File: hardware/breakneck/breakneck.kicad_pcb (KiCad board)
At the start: 2 copper layers, 53.3 x 64 mm, 117 parts, among them J1 CONN_WEST, J10 GS2, J12 CONN_JTAG_6P, J15 GS2, J16 CONN_JST, J2 CONN_DEDI, J3 CONN_OLED, J4 USB_C_Rcpt_Min, J5 CONN_SOUTH, J6 CONN_EAST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

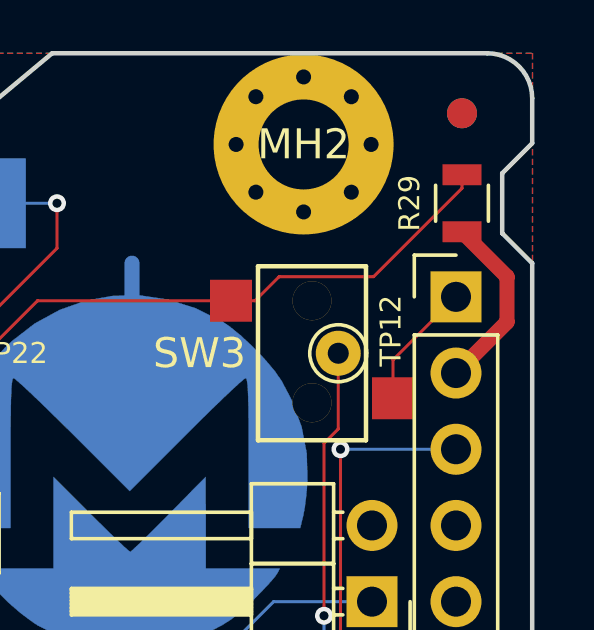
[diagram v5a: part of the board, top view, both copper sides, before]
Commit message: Corrected switching as VCI_IN0 is a wakeup or interrupt on active low.
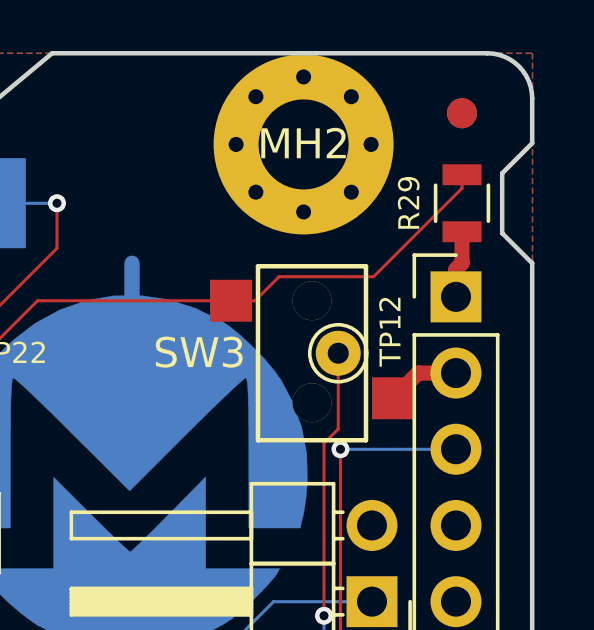
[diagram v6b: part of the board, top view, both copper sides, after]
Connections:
- R29 pad 1: +3V3 -> GND
- SW3 pad 2: GND -> +3V3
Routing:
- net +3V3: track 182.7 -> 179.1 mm
- net GND: track 226.8 -> 224.8 mm
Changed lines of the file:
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@@
     (fp_line (start 1.55 0.9) (end -1.55 0.9) (layer F.CrtYd) (width 0.05))
     (pad 1 smd rect (at -0.95 0 90) (size 0.7 1.3) (layers F.Cu F.Paste F.Mask)
-      (net 3 +3V3))
+      (net 1 GND))
     (pad 2 smd rect (at 0.95 0 90) (size 0.7 1.3) (layers F.Cu F.Paste F.Mask)
       (net 161 "Net-(R29-Pad2)"))
@@
       (net 161 "Net-(R29-Pad2)"))
     (pad 2 smd rect (at -1.5 2.7 90) (size 1.4 1.4) (layers F.Cu F.Paste F.Mask)
-      (net 1 GND))
+      (net 3 +3V3))
     (pad A thru_hole circle (at -1.65 0 90) (size 1.3 1.3) (drill 1.3) (layers *.Cu *.Mask))
     (pad B thru_hole circle (at 1.75 0 90) (size 1.3 1.3) (drill 1.3) (layers *.Cu *.Mask))
@@
   (segment (start 147 114.6) (end 147 113.5) (width 0.1016) (layer F.Cu) (net 1))
   (segment (start 144.5 114.6) (end 144.5 113.5) (width 0.1016) (layer F.Cu) (net 1))
-  (segment (start 148.7 75.5) (end 148.7 74.22) (width 0.1016) (layer F.Cu) (net 1))
-  (segment (start 148.7 74.22) (end 150.8 72.12) (width 0.1016) (layer F.Cu) (net 1))
   (segment (start 118.55 89.8726) (end 118.55 86.75) (width 0.508) (layer F.Cu) (net 1))
   (segment (start 123.6926 89.75) (end 125.045 91.1024) (width 0.1016) (layer B.Cu) (net 1))
@@
   (segment (start 146.75 123) (end 147 123.25) (width 0.1016) (layer B.Cu) (net 1))
   (segment (start 147.74 126.84) (end 147.74 123.99) (width 0.1016) (layer F.Cu) (net 1))
+  (segment (start 151 71) (end 151 69.95) (width 0.508) (layer F.Cu) (net 1))
+  (segment (start 150.8 72.12) (end 150.8 71.2) (width 0.508) (layer F.Cu) (net 1))
+  (segment (start 150.8 71.2) (end 151 71) (width 0.508) (layer F.Cu) (net 1))
   (via (at 132.8485 69) (size 0.6) (drill 0.3) (layers F.Cu B.Cu) (net 2))
   (segment (start 132.92 71.325) (end 132.92 69.0715) (width 0.1016) (layer B.Cu) (net 2) (status 10))
@@
   (segment (start 142.5 101.4) (end 141.352401 100.252401) (width 0.1016) (layer F.Cu) (net 3))
   (segment (start 141.352401 98.652401) (end 141.352401 101.897599) (width 0.1016) (layer F.Cu) (net 3))
-  (segment (start 150.8 74.66) (end 152.5 72.96) (width 0.508) (layer F.Cu) (net 3))
-  (segment (start 152.5 72.96) (end 152.5 71.45) (width 0.508) (layer F.Cu) (net 3))
-  (segment (start 152.5 71.45) (end 151 69.95) (width 0.508) (layer F.Cu) (net 3))
   (via (at 144.65 126.95) (size 0.6) (drill 0.3) (layers F.Cu B.Cu) (net 3))
   (segment (start 146 126.95) (end 144.65 126.95) (width 0.1016) (layer B.Cu) (net 3))
@@
   (segment (start 122.15 104.75) (end 122.5 105.1) (width 0.1016) (layer B.Cu) (net 3))
   (segment (start 118.114801 104.75) (end 122.15 104.75) (width 0.1016) (layer B.Cu) (net 3))
+  (segment (start 149.54 74.66) (end 148.7 75.5) (width 0.508) (layer F.Cu) (net 3))
+  (segment (start 150.8 74.66) (end 149.54 74.66) (width 0.508) (layer F.Cu) (net 3))
   (segment (start 139.5 112.4) (end 139.5 110.95) (width 0.1016) (layer F.Cu) (net 4) (status 30))
   (segment (start 119 80) (end 121.9976 77.0024) (width 0.1016) (layer B.Cu) (net 6) (status 10))

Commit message: Corrected incompatible SE (608A) timing in ROM assistance.
This follows advice taken from Microchip case 00347747, warning against
replacing the CEC1702 ROM addendum specification of ATECC508A with the
more capable ATECC608A SE.
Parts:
- U1: value ATECC608A -> ATECC508A
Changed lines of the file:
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@@
       (effects (font (size 1 1) (thickness 0.15)))
     )
-    (fp_text value ATECC608A (at 0 2.55 90) (layer F.Fab)
+    (fp_text value ATECC508A (at 0 2.55 90) (layer F.Fab)
       (effects (font (size 1 1) (thickness 0.15)))
     )

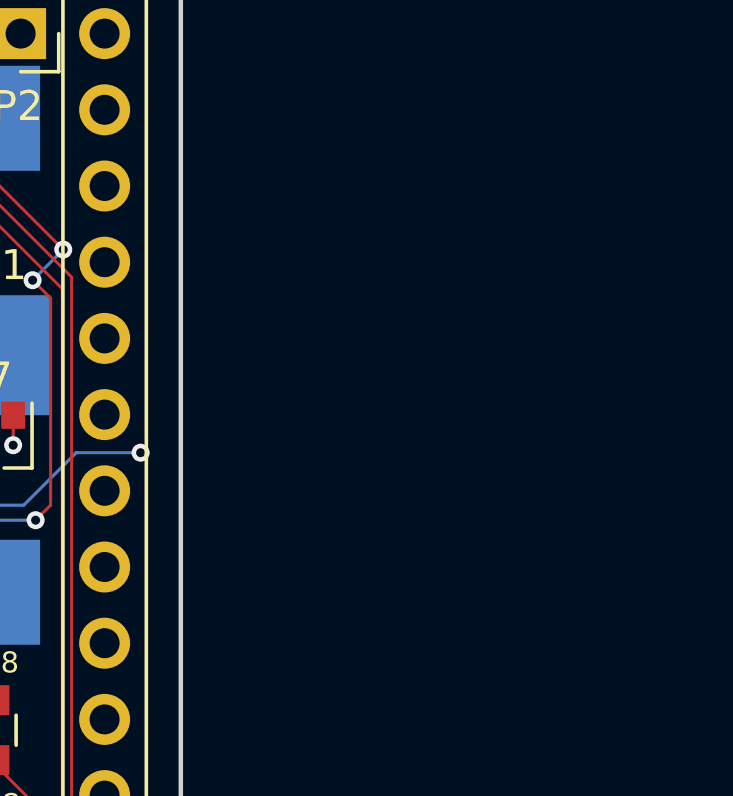
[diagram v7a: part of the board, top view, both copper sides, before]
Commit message: Prepared to integrate adjustable regulator and cleaned jumpers of paste.
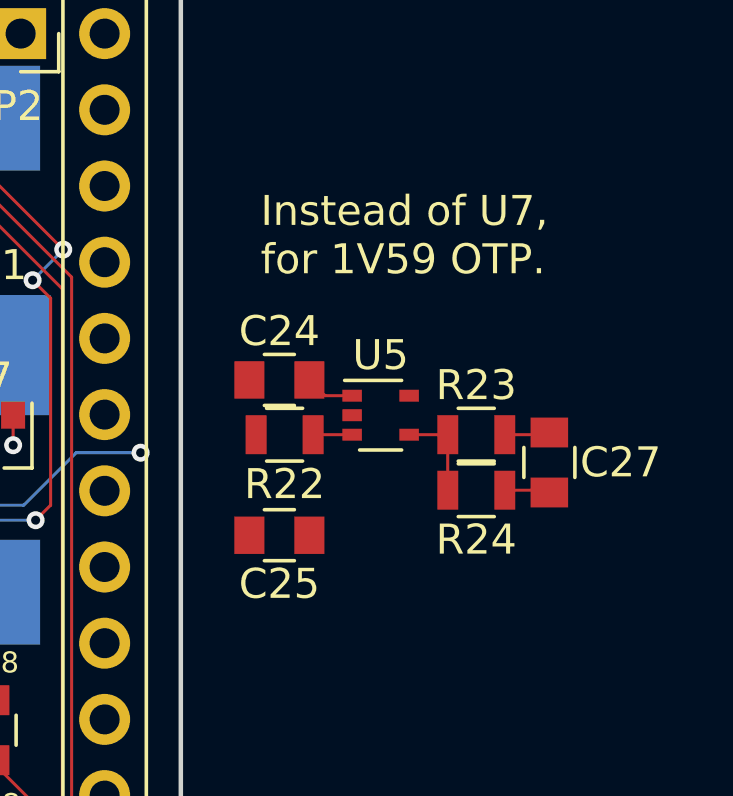
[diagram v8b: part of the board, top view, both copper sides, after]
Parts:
- added C24: 2.2uF, Monero_Local:C_0805, F.Cu at (156.6, 93.8)
- added C25: 100nF, Monero_Local:C_0805, F.Cu at (156.6, 99.0)
- added C27: 2.2uF, Monero_Local:C_0805, F.Cu at (165.6, 96.6)
- added R22: 1K, Monero_Local:R_0805, F.Cu at (156.8, 95.7)
- added R23: 130K, Monero_Local:R_0805, F.Cu at (163.2, 95.7)
- added R24: 220K, Monero_Local:R_0805, F.Cu at (163.2, 97.5)
- added U5: MIC5377YC5, Monero_Local:SOT-353_SC-70-5, F.Cu at (160.0, 95.0)
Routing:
- net Net-(R23-Pad2): track 0.00 -> 3.14 mm
- net +5V: track 138.2 -> 139.9 mm
- net GND: track 224.8 -> 226.2 mm
- net +1V5: track 21.5 -> 22.9 mm
- net Net-(R22-Pad2): track 0.00 -> 1.30 mm
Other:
- board text added: "Instead of U7, for 1V59 OTP."
